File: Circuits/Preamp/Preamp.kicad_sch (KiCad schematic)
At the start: 59 parts, among them J1 SMA, J2 MDM9S, U1 AD829AR, U2 REF43GS, U3 ADA4805-2ARMZ, U4 ADA4805-2ARMZ

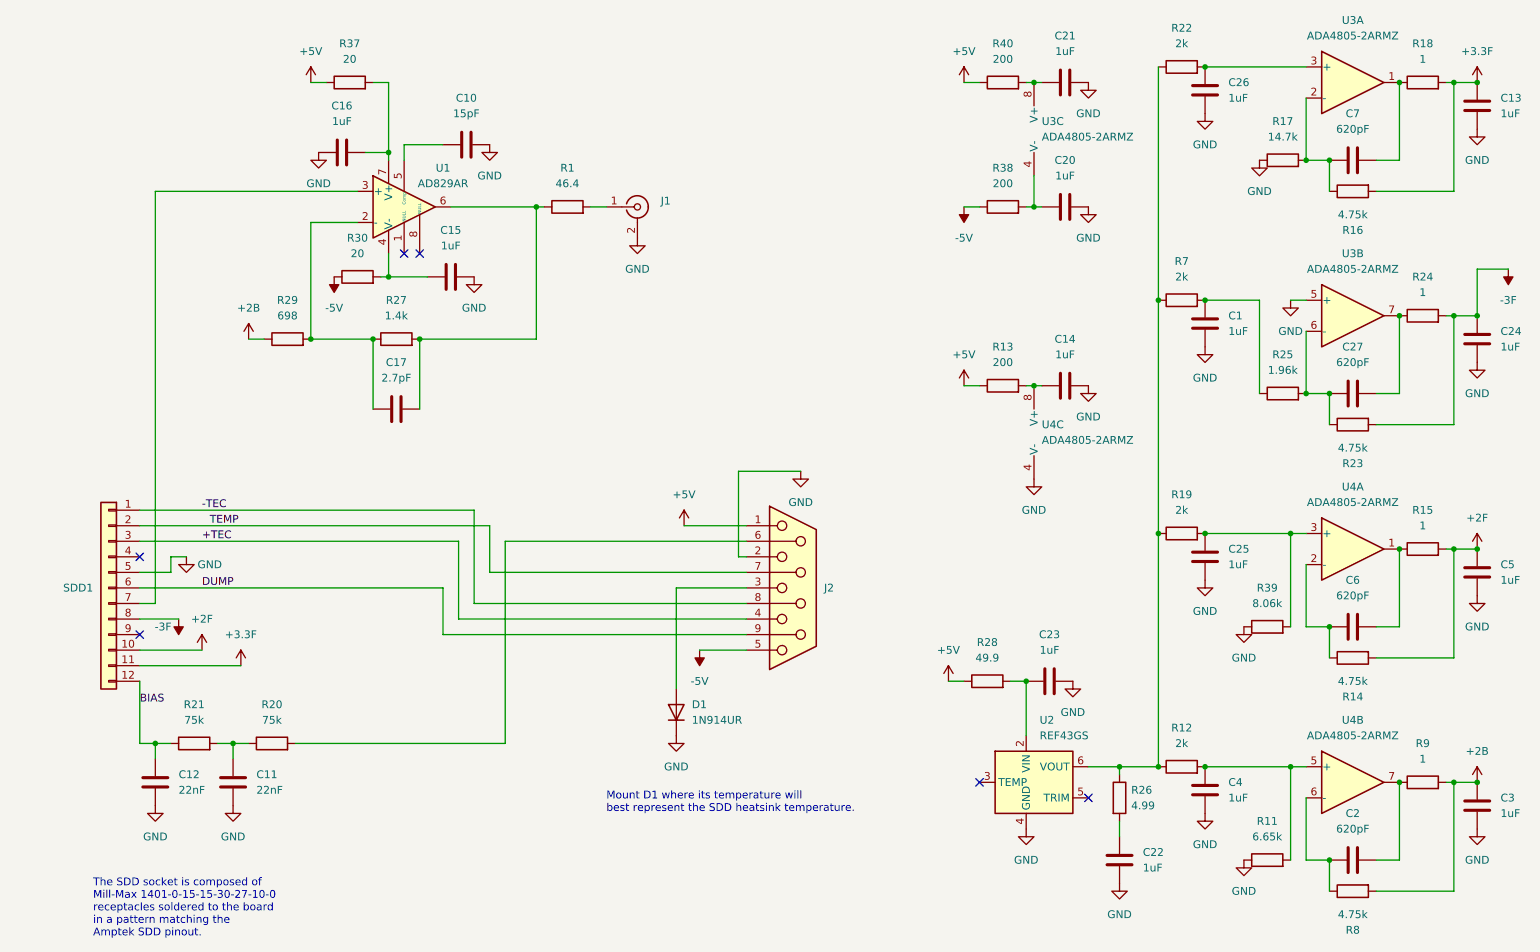
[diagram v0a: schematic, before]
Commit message: separate boards for detector and preamp
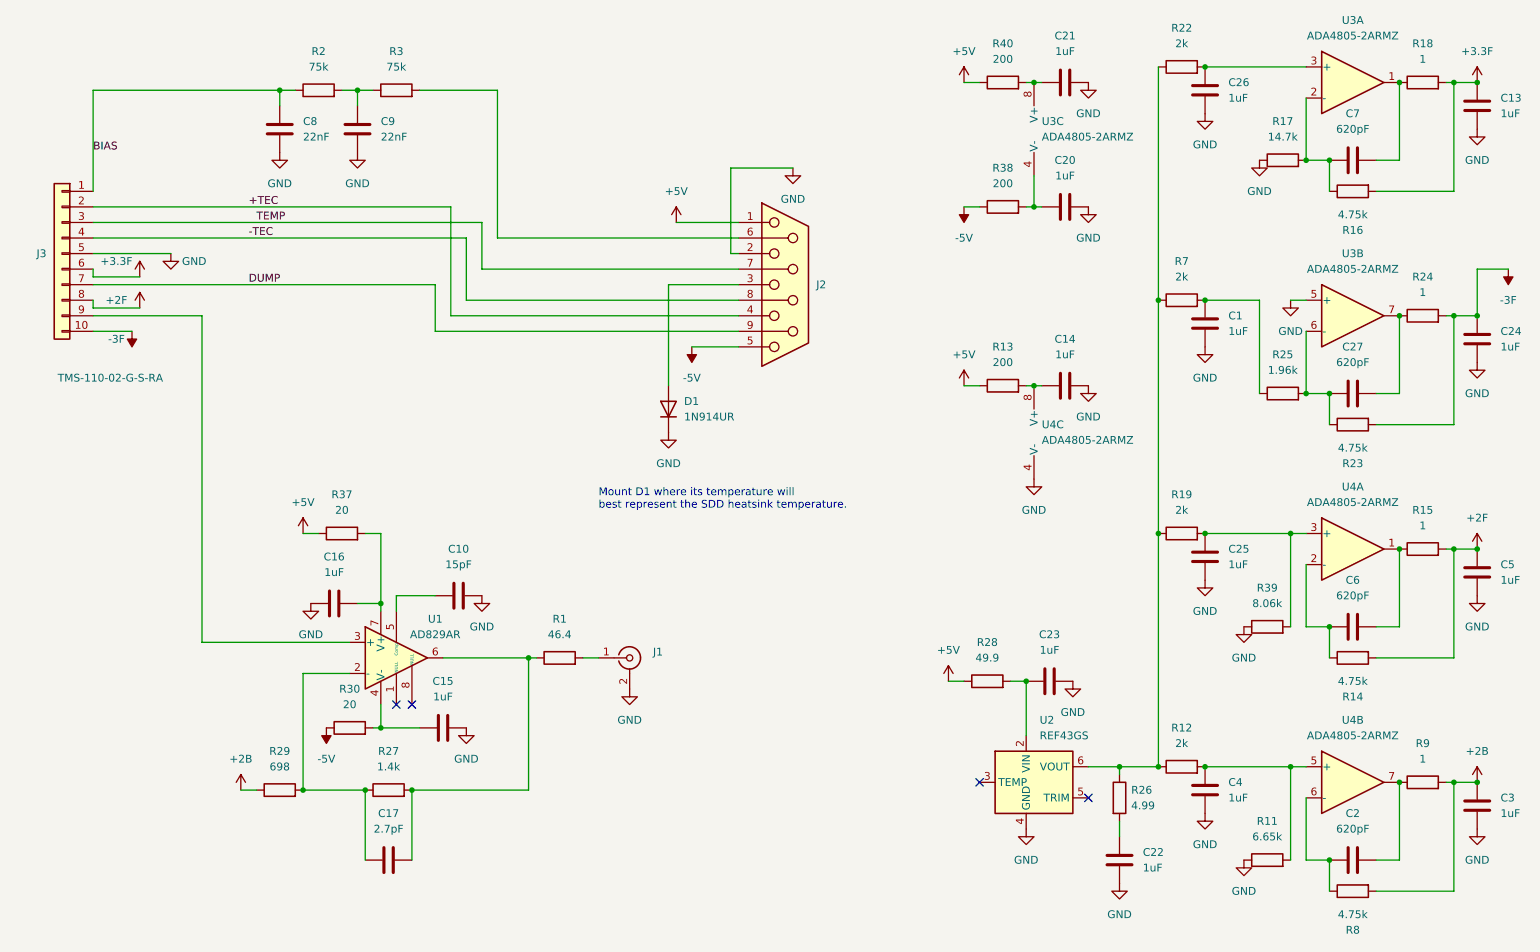
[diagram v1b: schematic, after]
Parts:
- removed C11, C12: 22nF, Capacitor_SMD:C_1210_3225Metric, symbol QuERI_symbols:Chv
- removed R20, R21: 75k, Resistor_SMD:R_0603_1608Metric, symbol QuERI_symbols:Rlowp
- removed SDD1: Conn_01x12, symbol Connector_Generic:Conn_01x12
- added C8, C9: 22nF, Capacitor_SMD:C_1210_3225Metric, symbol QuERI_symbols:Chv
- added J3: TMS-110-02-G-S-RA, Connector_PinHeader_1.27mm:PinHeader_1x10_P1.27mm_Horizontal, symbol Connector_Generic:Conn_01x10
- added R2, R3: 75k, Resistor_SMD:R_0603_1608Metric, symbol QuERI_symbols:Rlowp
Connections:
- net +2F: now also J3.8 (Pin_8)
- net +3.3F: now also J3.6 (Pin_6)
- net +TEC: now also J3.2 (Pin_2)
- net -3F: now also J3.10 (Pin_10)
- net -TEC: now also J3.4 (Pin_4)
- net BIAS: now also C8.1, J3.1 (Pin_1), R2.1
- net DUMP: now also J3.7 (Pin_7)
- net GND: now also C8.2, C9.2, J3.5 (Pin_5)
- net TEMP: now also J3.3 (Pin_3)
- net at J2.6: now also R3.2
- net at U1.3 (+): now also J3.9 (Pin_9)
- new net: C9.1, R2.2, R3.1
- no-connect marks 6 -> 4
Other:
- note removed: "The SDD socket is composed of Mill-Max 1401-0-15-15-30-27-10-0 receptacles soldered to the board in a pattern matching the Amptek SDD pinout."
- title: QuERI Focal Plane Module -> QuERI Preamplifier
- moved on the sheet: C10, C15, C16, C17, D1, J1, J2, R1, R27, R29, R30, R37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
